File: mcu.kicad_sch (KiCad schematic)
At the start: 83 parts, among them J1 USB_C, P20 HEADER-2x11, P22 HEADER-2x13, P26 LPC_JTAG, P28 HEADER-2x11, Q5 PMOS, SW1 SWITCH, SW2 SWITCH, U15 TVS_USB, U20 W25Q80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

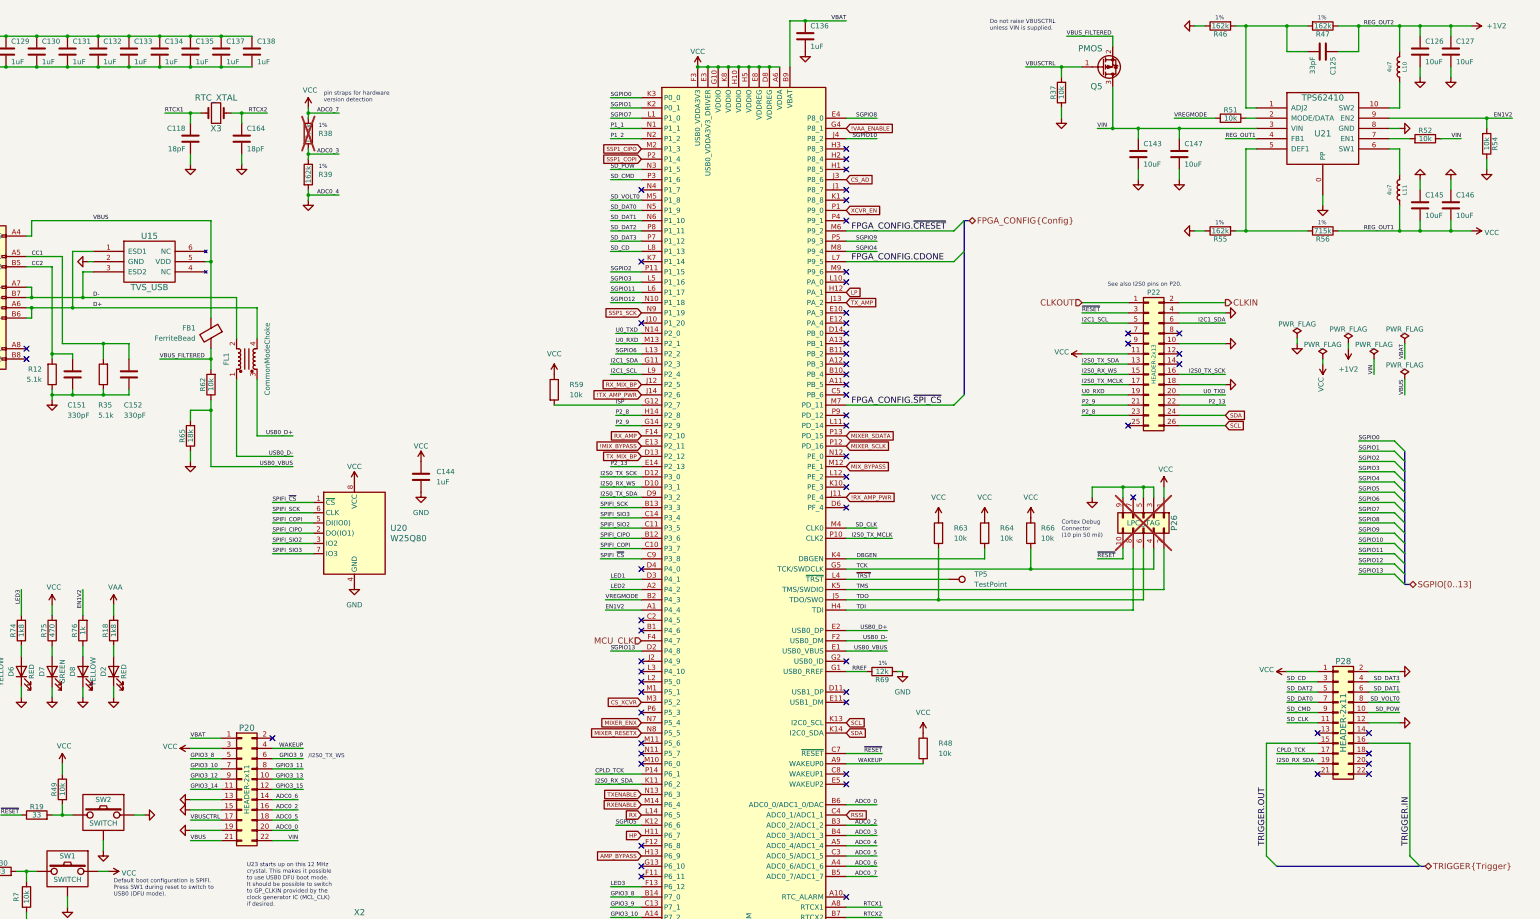
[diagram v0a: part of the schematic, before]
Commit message: Add overvoltage protection
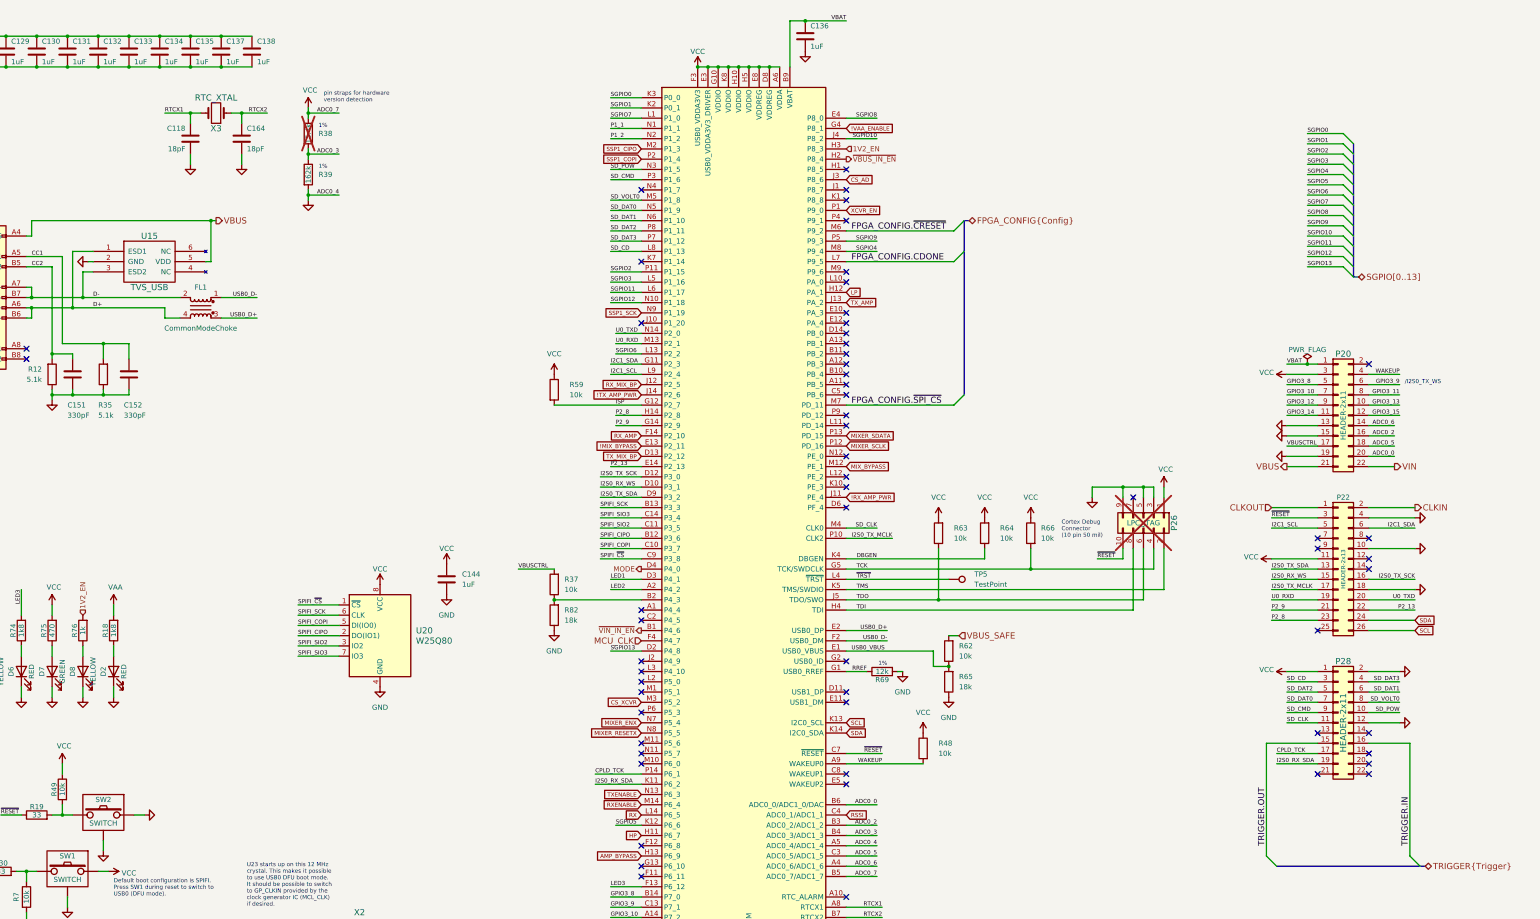
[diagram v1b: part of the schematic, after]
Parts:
- removed C125: 33pF, Capacitor_SMD:C_0201_0603Metric, symbol Device:C
- removed C126, C127, C143, C145, C146, C147: 10uF, Capacitor_SMD:C_0805_2012Metric, symbol Device:C
- removed FB1: FerriteBead, Inductor_SMD:L_0603_1608Metric, symbol Device:FerriteBead
- removed L10, L11: 4u7, Inductor_SMD:L_Taiyo-Yuden_NR-40xx, symbol Device:L
- removed Q5: PMOS, Package_TO_SOT_SMD:SOT-23-3, symbol Device:Q_PMOS_GSD
- removed R46, R47, R55: 162k, Resistor_SMD:R_0402_1005Metric, symbol Device:R
- removed R51, R52, R54: 10k, Resistor_SMD:R_0402_1005Metric, symbol Device:R
- removed R56: 715k, Resistor_SMD:R_0402_1005Metric, symbol Device:R
- removed U21: TPS62410, hackrf:GSG-S-PVSON-N10, symbol hackrf:TPS62410
- added R82: 18k, Resistor_SMD:R_0402_1005Metric, symbol Device:R
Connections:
- net GND: now also R82.1; no longer R37.1
- net ~{VIN_IN_EN}: now reaches U23.B1 (P4_6)
- net MODE: now reaches U23.D4 (P4_0)
- net ~{VBUS_IN_EN}: now reaches U23.H2 (P8_4)
- net 1V2_EN: now reaches U23.H3 (P8_3)
- net 1V2_EN: now also R76.2
- net EN1V2: no longer names the net of U23.A1 (P4_4)
- net EN1V2: no longer R76.2
- net VBUS_FILTERED renamed VBUS_SAFE
- net VREGMODE: no longer names the net of U23.B2 (P4_3)
- net VREGMODE: now also R37.1, R82.2
- no-connect marks 63 -> 60
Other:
- note removed: "Do not raise VBUSCTRL unless VIN is supplied."
- note removed: "See also I2S0 pins on P20."
- moved on the sheet: C144, FL1, P20, P22, R62, R65, U20

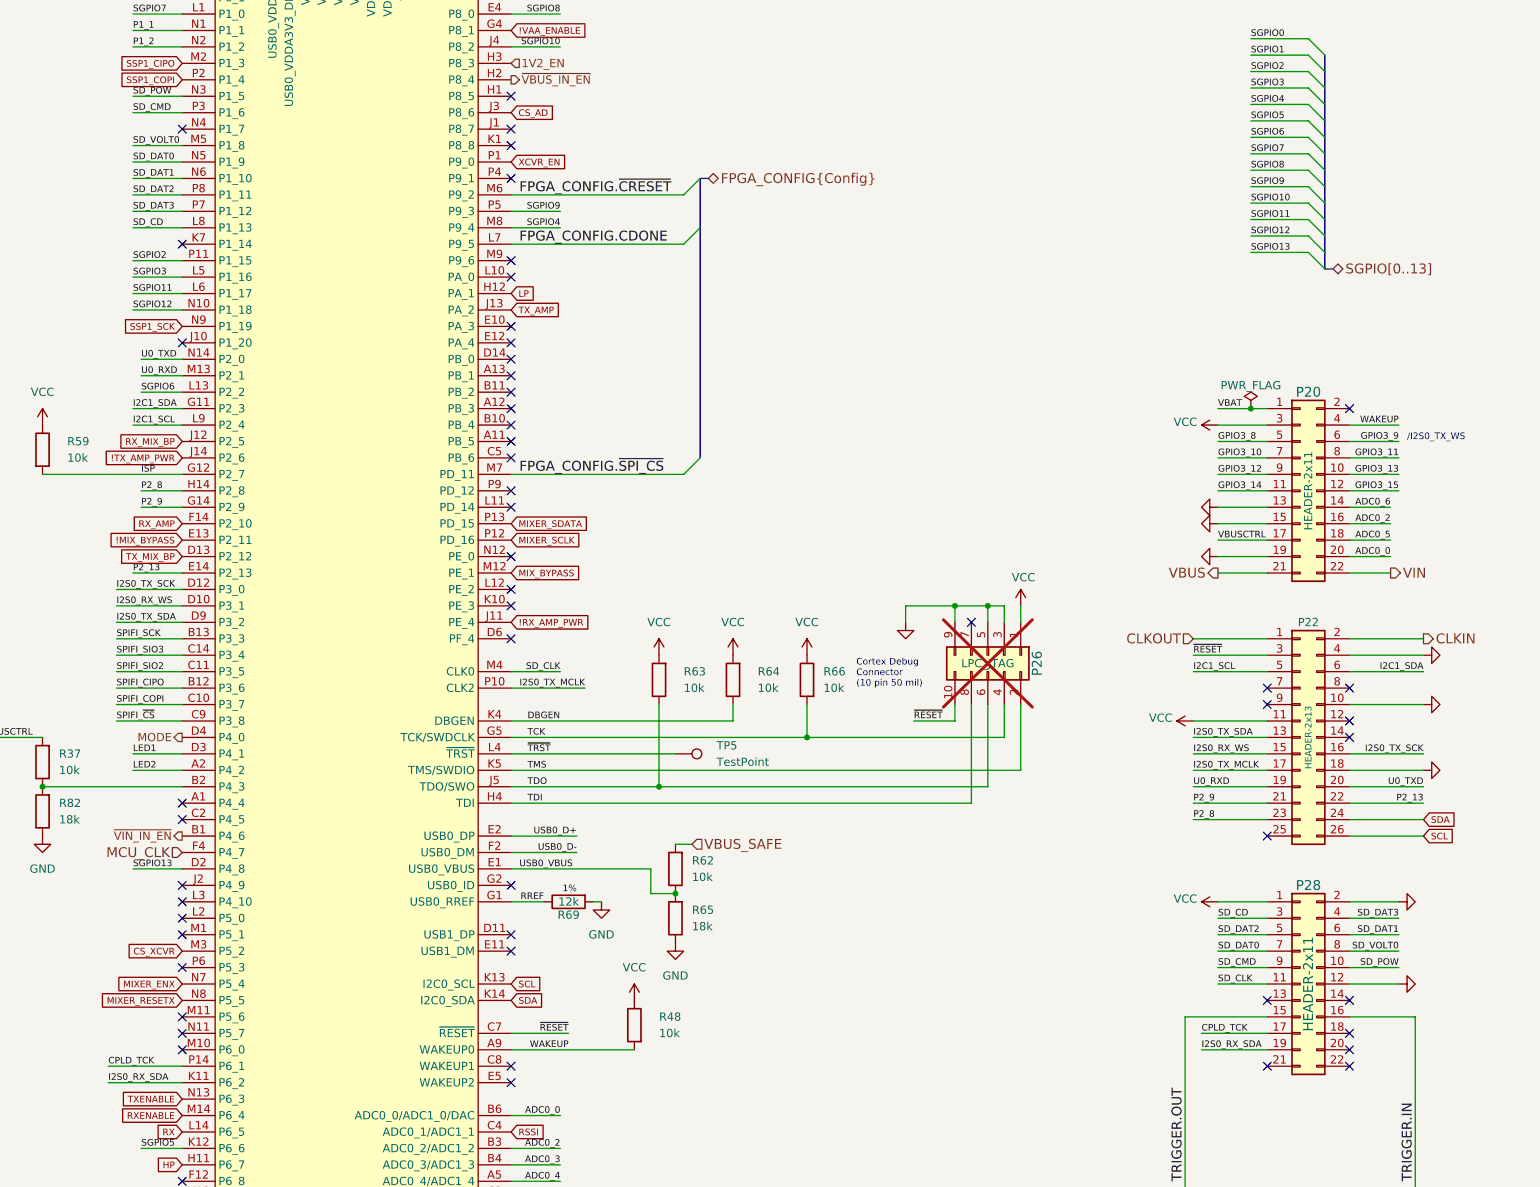
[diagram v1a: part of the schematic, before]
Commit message: Add more expansion pins
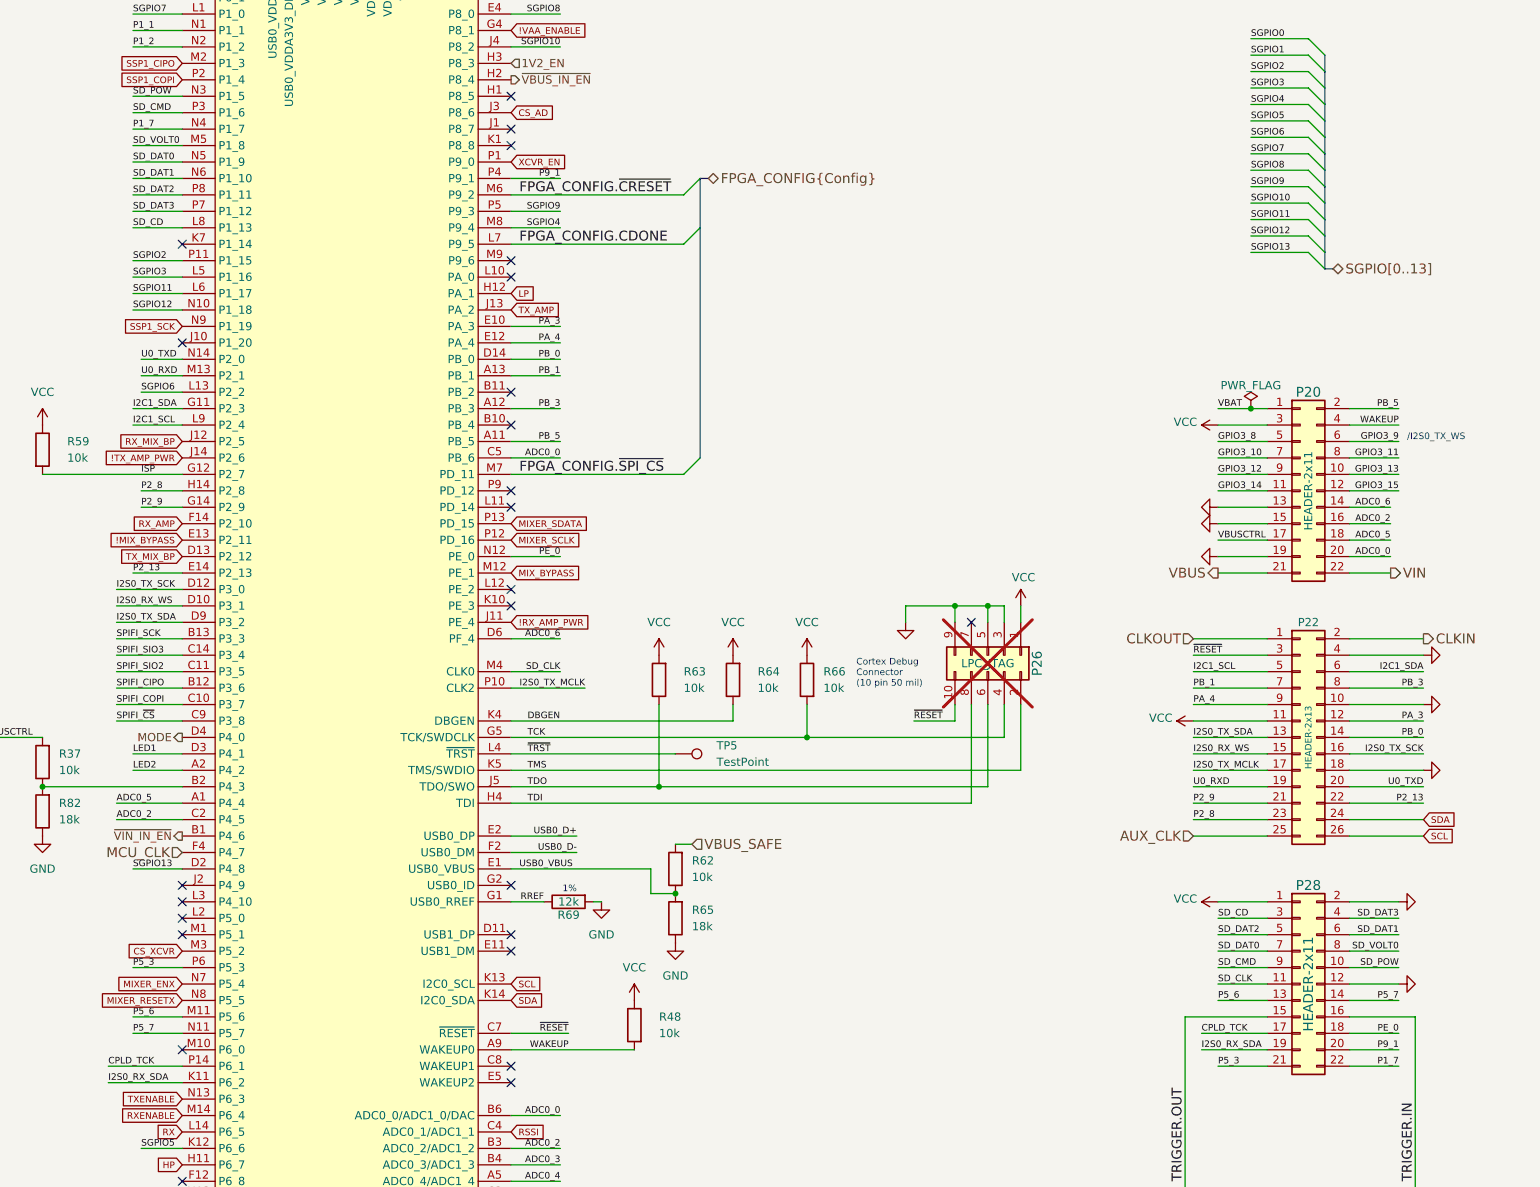
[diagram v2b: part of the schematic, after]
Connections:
- net ADC0_0: now also U23.C5 (PB_6)
- net ADC0_2: now also U23.C2 (P4_5)
- net ADC0_5: now also U23.A1 (P4_4)
- net ADC0_6: now also U23.D6 (PF_4)
- net P5_6: now reaches P28.13 (Pin_13)
- net P5_6: now also U23.M11 (P5_6)
- net P5_7: now reaches P28.14 (Pin_14)
- net P5_7: now also U23.N11 (P5_7)
- net PE_0: now reaches P28.18 (Pin_18)
- net PE_0: now also U23.N12 (PE_0)
- net P9_1: now reaches P28.20 (Pin_20)
- net P9_1: now also U23.P4 (P9_1)
- net P5_3: now reaches P28.21 (Pin_21)
- net P5_3: now also U23.P6 (P5_3)
- net P1_7: now reaches P28.22 (Pin_22)
- net P1_7: now also U23.N4 (P1_7)
- net PB_5: now reaches P20.2 (Pin_2)
- net PB_5: now also U23.A11 (PB_5)
- net PA_3: now reaches P22.12 (Pin_12)
- net PA_3: now also U23.E10 (PA_3)
- net PB_0: now reaches P22.14 (Pin_14)
- net PB_0: now also U23.D14 (PB_0)
- net AUX_CLK: now reaches P22.25 (Pin_25)
- net PB_1: now reaches P22.7 (Pin_7)
- net PB_1: now also U23.A13 (PB_1)
- net PB_3: now reaches P22.8 (Pin_8)
- net PB_3: now also U23.A12 (PB_3)
- net PA_4: now reaches P22.9 (Pin_9)
- net PA_4: now also U23.E12 (PA_4)
- no-connect marks 60 -> 31
